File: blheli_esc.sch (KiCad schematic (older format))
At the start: 45 parts, among them J1 Conn_01x03_Male, Q1 BC847, Q2 BC847, Q3 BC847, U1 AP1509, U2 EFM8BB21F16G

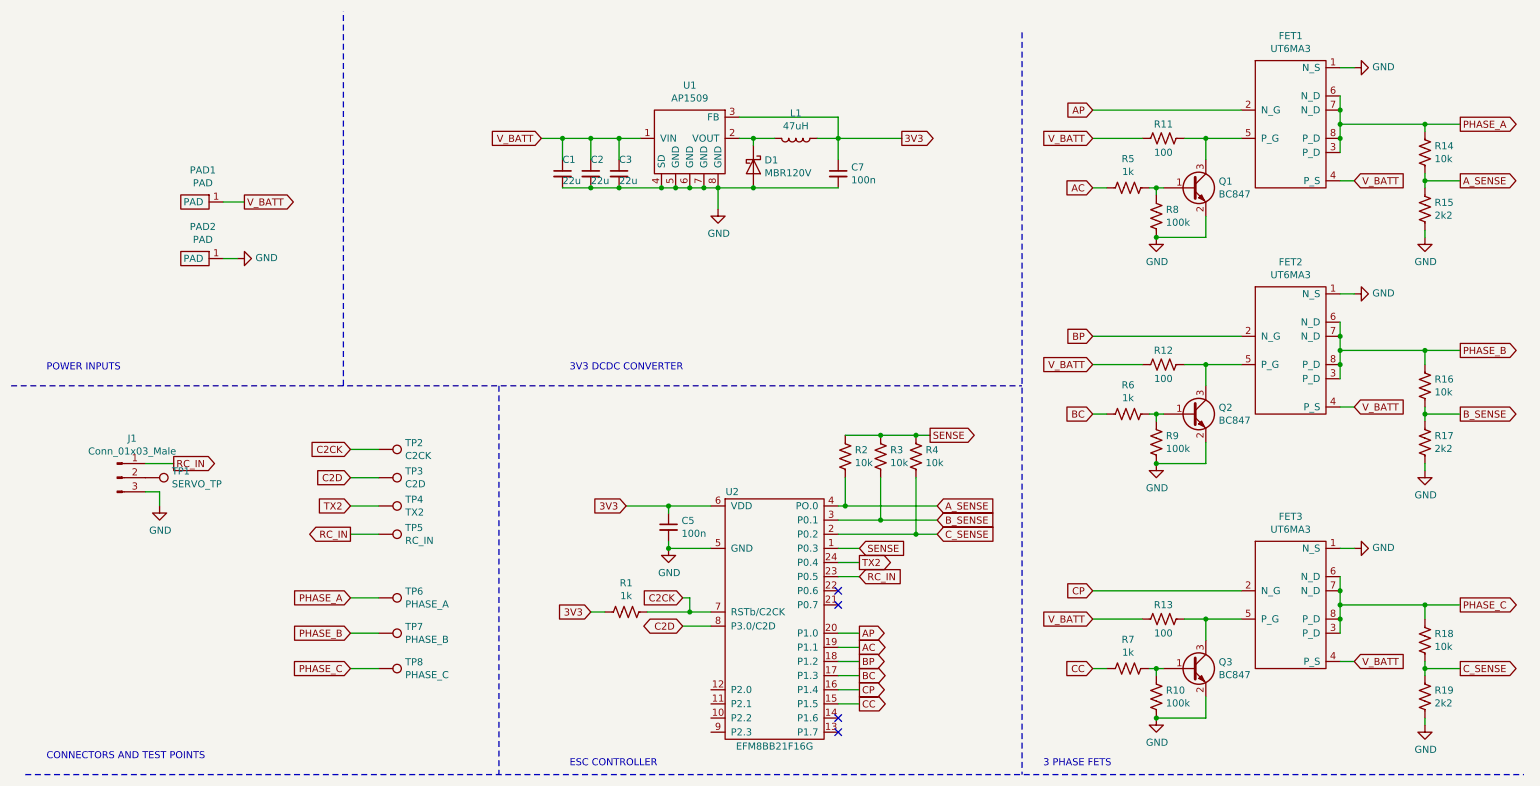
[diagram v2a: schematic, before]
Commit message: new design with easier to solder fets. 4 layer board
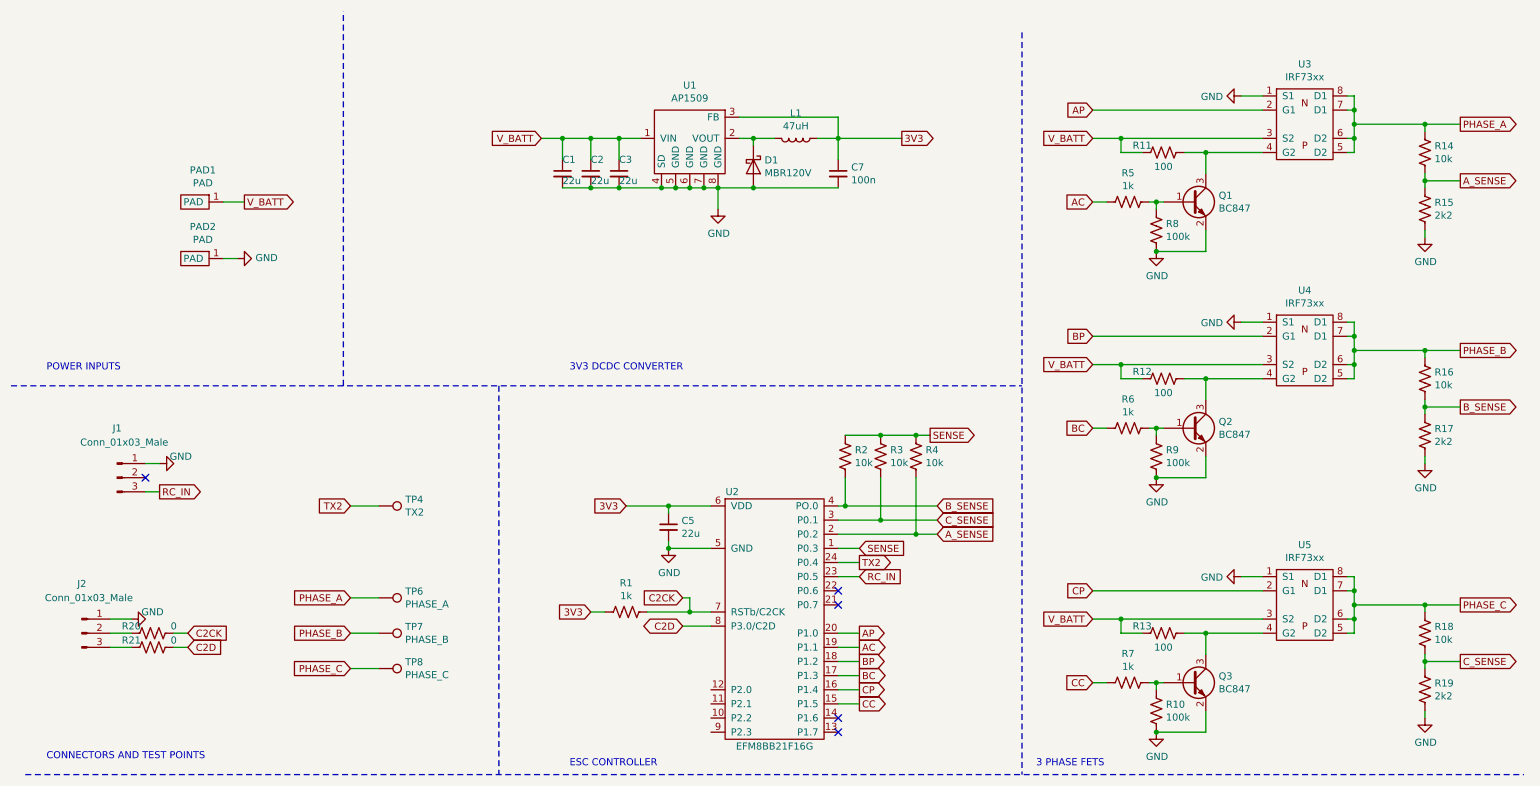
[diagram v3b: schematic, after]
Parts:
- removed FET1, FET2, FET3: UT6MA3, blheli_esc:UT6MA3, symbol blheli_esc:UT6MA3
- removed TP1: SERVO_TP, TestPoint:TestPoint_THTPad_D1.0mm_Drill0.5mm, symbol Connector:TestPoint
- removed TP2: C2CK, TestPoint:TestPoint_THTPad_D1.0mm_Drill0.5mm, symbol Connector:TestPoint
- removed TP3: C2D, TestPoint:TestPoint_THTPad_D1.0mm_Drill0.5mm, symbol Connector:TestPoint
- removed TP5: RC_IN, TestPoint:TestPoint_THTPad_D1.0mm_Drill0.5mm, symbol Connector:TestPoint
- added J2: Conn_01x03_Male, Connector_PinHeader_2.54mm:PinHeader_1x03_P2.54mm_Vertical, symbol Connector:Conn_01x03_Male
- added R20, R21: 0, Resistor_SMD:R_0603_1608Metric, symbol Device:R_US
- added U3, U4, U5: IRF73xx, blheli_esc:IRF7317PbF, symbol blheli_esc:IRF73xx
- C5: value 100n -> 22u
- TP6, TP7, TP8: footprint TestPoint:TestPoint_Pad_1.5x1.5mm -> TestPoint:TestPoint_Pad_3.0x3.0mm
- U2: footprint (none) -> blheli_esc:efm8b21-qsop24
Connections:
- net AP: now also U3.2 (G1)
- net A_SENSE: now also R4.1, U2.2 (P0.2); no longer R2.1, U2.4 (PO.0)
- net BP: now also U4.2 (G1)
- net B_SENSE: now also R2.1, U2.4 (PO.0); no longer R3.1, U2.3 (P0.1)
- net C2CK: now also R20.1
- net C2D: now also R21.1
- net CP: now also U5.2 (G1)
- net C_SENSE: now also R3.1, U2.3 (P0.1); no longer R4.1, U2.2 (P0.2)
- net GND: now also J1.1 (Pin_1), J2.1 (Pin_1), U3.1 (S1), U4.1 (S1), U5.1 (S1); no longer J1.3 (Pin_3)
- net PHASE_A: now also U3.5 (D2), U3.6 (D2), U3.7 (D1), U3.8 (D1)
- net PHASE_B: now also U4.5 (D2), U4.6 (D2), U4.7 (D1), U4.8 (D1)
- net PHASE_C: now also U5.5 (D2), U5.6 (D2), U5.7 (D1), U5.8 (D1)
- net RC_IN: now also J1.3 (Pin_3); no longer J1.1 (Pin_1)
- net V_BATT: now also U3.3 (S2), U4.3 (S2), U5.3 (S2)
- net at Q1.3 (C), R11.1: now also U3.4 (G2)
- net at Q2.3 (C), R12.1: now also U4.4 (G2)
- net at Q3.3 (C), R13.1: now also U5.4 (G2)
- new net: J2.2 (Pin_2), R20.2
- new net: J2.3 (Pin_3), R21.2
- no-connect marks 4 -> 5
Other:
- moved on the sheet: Q1, R11, R5, R8
